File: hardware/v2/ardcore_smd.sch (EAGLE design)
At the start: 78 parts, among them IC10 TL072, IC11 74AHCT1G125DBV, IC2 7805DT, IC4 4921, IC5 74AHCT1G125DBV, IC6 ATMEGA328P-AU, IC7 74AHCT1G125DBV, IC8 74AHCT1G125DBV, Y1 RESONATORSMD

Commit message: New components
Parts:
- removed AUDIO_OUT: WQP-PJ301M-12_JACK, thonkiconn:WQP-PJ301M-12_JACK
- removed C21: 100p, rcl:C-USC0603
- removed C29: 47p, rcl:C-USC0603
- removed IC10: TL072, linear:TL072D
- removed R45, R46: 39k, rcl:R-US_R0603
- removed R50: 47k, rcl:R-US_R0603
- removed R55: 1.0k, rcl:R-US_R0603
- removed R56: 100k, rcl:R-US_R0603
- added AUDIO_OUT1, AUDIO_OUT2: WQP-PJ301M-12_JACK, thonkiconn:WQP-PJ301M-12_JACK
- added C11: 470n, rcl:C-USC0603
- added C14, C15, C19, C20: 220p, rcl:C-USC0603
- added C17, C23: 18p, rcl:C-USC0603
- added C8, C9: 100n, rcl:C-USC0603
- added IC1, IC3: OPA2171, linear:TL072D
- added IC12: LM4040B25, texas:LM4041B12DBZ
- added IC9: LM4040B10, texas:LM4041B12DBZ
- added L1: (no value), wuerth-elektronik:WE-CBF_0603
- added R12, R14, R17, R22, R24, R26: 39k, rcl:R-US_R0603
- added R18, R29: 249k, rcl:R-US_R0603
- added R19, R30: 309k, rcl:R-US_R0603
- added R20, R31: 1.0k, rcl:R-US_R0603
- added R25, R9: 3.3k, rcl:R-US_R0603
- added U2: DAC8552IDGKT, Texas Instruments_By_element14_Batch_1:DAC8552IDGKT
- C22: value 100p -> 470n
- C4: value 10u -> 22u; device rcl:CPOL-EUE2.5-5 -> rcl:CPOL-USC
- IC4: value 4921 -> LM1117-3.3; device adafruit_mcp:MCP4921SO08 -> og-vreg:REG1117
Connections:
- removed net N$67: C21.2, C4.+, IC10B.-IN, IC10B.OUT
- removed net N$68: C4.-, R50.2
- removed net N$69: C22.1, IC10B.+IN, R46.1
- removed net N$71: C21.1, R45.1, R46.2
- removed net N$72: AUDIO_OUT.2, R55.1, R56.1
- removed net N$73: C29.2, IC10A.OUT, R55.2
- removed net N$75: C29.1, IC10A.-IN, R50.1, R56.2
- new net +3V3: C4.+, C8.1, IC4.VOUT, L1.1
- new net +3V3_A: C9.1, L1.2, R9.1, U2.VDD
- new net A: R22.2, U2.VOUTA
- new net AREF_-10: C22.1, IC9.A, R19.2, R25.2, R30.2
- new net AREF_2.5: C11.1, IC12.C, R9.2, U2.VREF
- new net B: R12.2, U2.VOUTB
- new net BI_OUT: C17.2, IC1A.OUT, R18.1, R20.2
- new net BI_OUT1: C23.2, IC3A.OUT, R29.1, R31.2
- new net F_CV: C17.1, IC1A.-IN, R17.1, R18.2, R19.1
- new net F_CV1: C23.1, IC3A.-IN, R26.1, R29.2, R30.1
- new net N$1: C14.1, R12.1, R14.2
- new net N$24: C20.1, IC3B.+IN, R24.1
- new net N$26: C19.1, R22.1, R24.2
- new net N$32: AUDIO_OUT1.2, R31.1
- new net N$4: C19.2, IC3B.-IN, IC3B.OUT, R26.2
- new net N$42: C14.2, IC1B.-IN, IC1B.OUT, R17.2
- new net N$43: C15.1, IC1B.+IN, R14.1
- net +5V: no longer IC4.REFA, IC4.VDD
- net GND: now also AUDIO_OUT1.1, AUDIO_OUT2.1, C11.2, C15.2, C20.2, C4.-, C8.2, C9.2, IC12.A, IC1A.+IN, IC3A.+IN, IC4.GND, IC9.C, U2.GND; no longer AUDIO_OUT.1, IC10A.+IN, IC4.AVSS, IC4.LDAC
- net MOSI: no longer IC4.SDI
- net N$2: now also AUDIO_OUT2.2, R20.1; no longer IC4.DACA, R45.2
- net SCK: no longer IC4.SCK
- net SS: no longer IC4.#CS
- net VCC: now also IC1P.V+, IC3P.V+, IC4.VIN; no longer IC10P.V+
- net VEE: now also IC1P.V-, IC3P.V-, R25.1; no longer IC10P.V-
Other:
- note added: "+/-8V"
- note removed: "DAC alternatives: MCP4901 8bit MCP4911 10bit MCP4921 12bit"

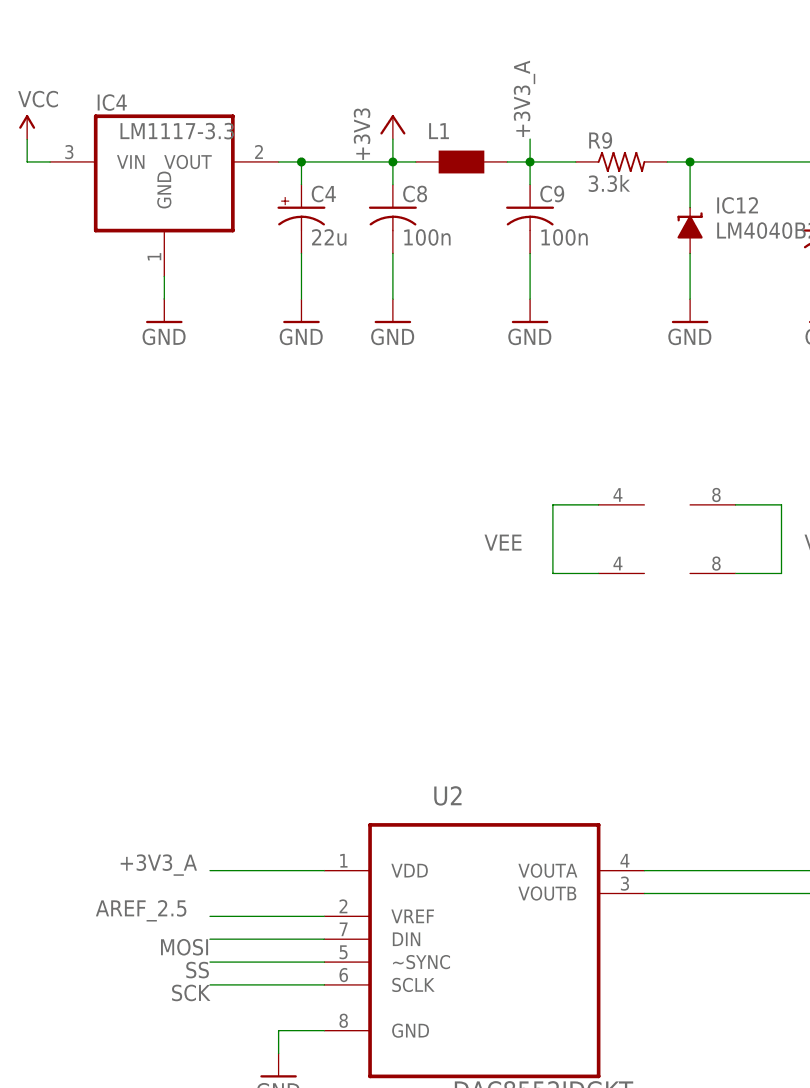
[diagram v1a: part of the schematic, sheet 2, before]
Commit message: removing 3v3 reg
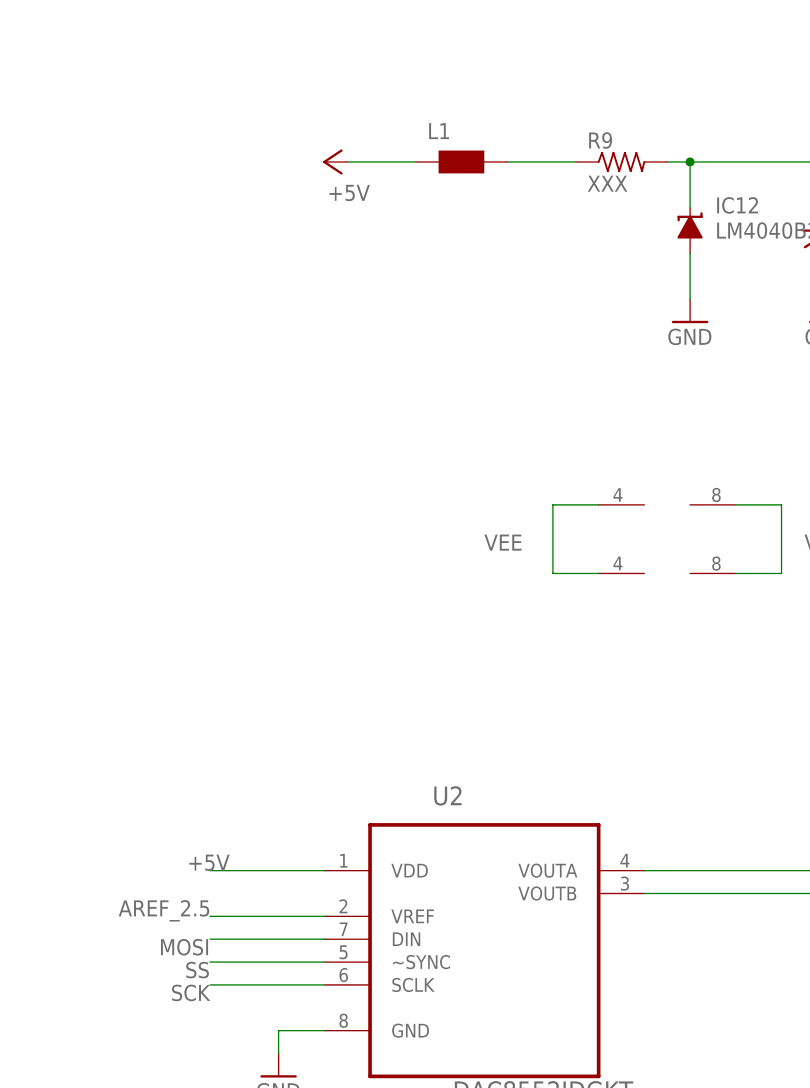
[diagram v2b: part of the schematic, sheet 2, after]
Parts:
- removed C4: 22u, rcl:CPOL-USC
- removed C8, C9: 100n, rcl:C-USC0603
- removed IC4: LM1117-3.3, og-vreg:REG1117
- R9: value 3.3k -> XXX
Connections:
- removed net +3V3: C4.+, C8.1, IC4.VOUT, L1.1
- removed net +3V3_A: C9.1, L1.2, R9.1, U2.VDD
- new net N$33: L1.2, R9.1
- net +5V: now also L1.1, U2.VDD
- net GND: no longer C4.-, C8.2, C9.2, IC4.GND
- net VCC: no longer IC4.VIN
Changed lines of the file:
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@@
 <?xml version="1.0" encoding="utf-8"?>
 <!DOCTYPE eagle SYSTEM "eagle.dtd">
-<eagle version="6.1">
+<eagle version="7.3.0">
 <drawing>
 <settings>
@@
 <part name="GND4" library="SparkFun" deviceset="GND" device=""/>
 <part name="GND14" library="SparkFun" deviceset="GND" device=""/>
-<part name="C4" library="rcl" deviceset="CPOL-US" device="C" value="22u"/>
-<part name="C8" library="rcl" deviceset="C-US" device="C0603" value="100n"/>
-<part name="GND16" library="SparkFun" deviceset="GND" device=""/>
-<part name="GND18" library="SparkFun" deviceset="GND" device=""/>
-<part name="GND36" library="SparkFun" deviceset="GND" device=""/>
-<part name="IC4" library="og-vreg" deviceset="REG1117" device="" value="LM1117-3.3"/>
-<part name="+3V1" library="supply1" deviceset="+3V3" device=""/>
-<part name="P+4" library="SparkFun" deviceset="VCC" device=""/>
 <part name="L1" library="wuerth-elektronik" deviceset="WE-CBF" device="_0603"/>
-<part name="C9" library="rcl" deviceset="C-US" device="C0603" value="100n"/>
-<part name="GND23" library="SparkFun" deviceset="GND" device=""/>
 <part name="IC9" library="texas" deviceset="LM4041" device="DBZ" technology="B12" value="LM4040B10"/>
 <part name="R25" library="rcl" deviceset="R-US_" device="R0603" value="3.3k"/>
@@
 <part name="SUPPLY3" library="supply2" deviceset="VEE" device=""/>
 <part name="IC12" library="texas" deviceset="LM4041" device="DBZ" technology="B12" value="LM4040B25"/>
-<part name="R9" library="rcl" deviceset="R-US_" device="R0603" value="3.3k"/>
+<part name="R9" library="rcl" deviceset="R-US_" device="R0603" value="XXX"/>
 <part name="GND24" library="SparkFun" deviceset="GND" device=""/>
 <part name="C11" library="rcl" deviceset="C-US" device="C0603" value="470n"/>
 <part name="GND25" library="SparkFun" deviceset="GND" device=""/>
 <part name="GND31" library="SparkFun" deviceset="GND" device=""/>
+<part name="P+10" library="supply1" deviceset="+5V" device=""/>
 </parts>
 <sheets>
@@
 <instance part="GND4" gate="1" x="233.68" y="71.12"/>
 <instance part="GND14" gate="1" x="236.22" y="10.16"/>
-<instance part="C4" gate="G$1" x="40.64" y="139.7"/>
-<instance part="C8" gate="G$1" x="50.8" y="139.7"/>
-<instance part="GND16" gate="1" x="25.4" y="127"/>
-<instance part="GND18" gate="1" x="40.64" y="127"/>
-<instance part="GND36" gate="1" x="50.8" y="127"/>
-<instance part="IC4" gate="G$1" x="25.4" y="144.78"/>
-<instance part="+3V1" gate="G$1" x="50.8" y="149.86"/>
-<instance part="P+4" gate="1" x="10.16" y="147.32"/>
 <instance part="L1" gate="G$1" x="58.42" y="142.24"/>
-<instance part="C9" gate="G$1" x="66.04" y="139.7"/>
-<instance part="GND23" gate="1" x="66.04" y="127"/>
 <instance part="IC9" gate="G$1" x="149.86" y="129.54" rot="R180"/>
 <instance part="R25" gate="G$1" x="149.86" y="144.78" rot="R270"/>
@@
 <instance part="IC3" gate="P" x="81.28" y="106.68" rot="R270"/>
 <instance part="IC1" gate="P" x="81.28" y="99.06" rot="R270"/>
+<instance part="P+10" gate="1" x="43.18" y="144.78" rot="R90"/>
 </instances>
 <busses>
@@
 <pinref part="AUDIO_OUT1" gate="G$1" pin="1"/>
 <wire x1="233.68" y1="78.74" x2="238.76" y2="78.74" width="0.1524" layer="91"/>
-</segment>
-<segment>
-<wire x1="25.4" y1="132.08" x2="25.4" y2="129.54" width="0.1524" layer="91"/>
-<pinref part="GND16" gate="1" pin="GND"/>
-<pinref part="IC4" gate="G$1" pin="GND"/>
-</segment>
-<segment>
-<wire x1="40.64" y1="134.62" x2="40.64" y2="129.54" width="0.1524" layer="91"/>
-<pinref part="C4" gate="G$1" pin="-"/>
-<pinref part="GND18" gate="1" pin="GND"/>
-</segment>
-<segment>
-<wire x1="50.8" y1="134.62" x2="50.8" y2="129.54" width="0.1524" layer="91"/>
-<pinref part="C8" gate="G$1" pin="2"/>
-<pinref part="GND36" gate="1" pin="GND"/>
-</segment>
-<segment>
-<wire x1="66.04" y1="134.62" x2="66.04" y2="129.54" width="0.1524" layer="91"/>
-<pinref part="C9" gate="G$1" pin="2"/>
-<pinref part="GND23" gate="1" pin="GND"/>
 </segment>
 <segment>
@@
 <net name="VCC" class="0">
 <segment>
-<wire x1="10.16" y1="144.78" x2="12.7" y2="144.78" width="0.1524" layer="91"/>
-<wire x1="10.16" y1="147.32" x2="10.16" y2="144.78" width="0.1524" layer="91"/>
-<pinref part="IC4" gate="G$1" pin="VIN"/>
-<pinref part="P+4" gate="1" pin="VCC"/>
-</segment>
-<segment>
 <pinref part="IC3" gate="P" pin="V+"/>
 <wire x1="88.9" y1="106.68" x2="93.98" y2="106.68" width="0.1524" layer="91"/>
@@
 <wire x1="88.9" y1="99.06" x2="93.98" y2="99.06" width="0.1524" layer="91"/>
 <wire x1="93.98" y1="99.06" x2="93.98" y2="106.68" width="0.1524" layer="91"/>
-</segment>
-</net>
-<net name="+3V3" class="0">
-<segment>
-<wire x1="38.1" y1="144.78" x2="40.64" y2="144.78" width="0.1524" layer="91"/>
-<wire x1="40.64" y1="144.78" x2="50.8" y2="144.78" width="0.1524" layer="91"/>
-<wire x1="40.64" y1="142.24" x2="40.64" y2="144.78" width="0.1524" layer="91"/>
-<wire x1="50.8" y1="147.32" x2="50.8" y2="144.78" width="0.1524" layer="91"/>
-<wire x1="53.34" y1="144.78" x2="50.8" y2="144.78" width="0.1524" layer="91"/>
-<wire x1="50.8" y1="142.24" x2="50.8" y2="144.78" width="0.1524" layer="91"/>
-<junction x="40.64" y="144.78"/>
-<junction x="50.8" y="144.78"/>
-<pinref part="C4" gate="G$1" pin="+"/>
-<pinref part="IC4" gate="G$1" pin="VOUT"/>
-<pinref part="+3V1" gate="G$1" pin="+3V3"/>
-<pinref part="L1" gate="G$1" pin="1"/>
-<pinref part="C8" gate="G$1" pin="1"/>
-</segment>
-</net>
-<net name="+3V3_A" class="0">
-<segment>
-<wire x1="63.5" y1="144.78" x2="66.04" y2="144.78" width="0.1524" layer="91"/>
-<wire x1="66.04" y1="144.78" x2="66.04" y2="142.24" width="0.1524" layer="91"/>
-<wire x1="66.04" y1="144.78" x2="66.04" y2="147.32" width="0.1524" layer="91"/>
-<wire x1="71.12" y1="144.78" x2="66.04" y2="144.78" width="0.1524" layer="91"/>
-<junction x="66.04" y="144.78"/>
-<label x="66.04" y="147.32" size="1.778" layer="95" rot="R90"/>
-<pinref part="L1" gate="G$1" pin="2"/>
-<pinref part="C9" gate="G$1" pin="1"/>
-<pinref part="R9" gate="G$1" pin="1"/>
-</segment>
-<segment>
-<pinref part="U2" gate="A" pin="VDD"/>
-<wire x1="43.18" y1="66.04" x2="30.48" y2="66.04" width="0.1524" layer="91"/>
-<label x="20.32" y="66.04" size="1.778" layer="95"/>
 </segment>
 </net>
@@
 <pinref part="U2" gate="A" pin="VREF"/>
 <wire x1="43.18" y1="60.96" x2="30.48" y2="60.96" width="0.1524" layer="91"/>
-<label x="17.78" y="60.96" size="1.778" layer="95"/>
+<label x="20.32" y="60.96" size="1.778" layer="95"/>
+</segment>
+</net>
+<net name="+5V" class="0">
+<segment>
+<pinref part="P+10" gate="1" pin="+5V"/>
+<pinref part="L1" gate="G$1" pin="1"/>
+<wire x1="45.72" y1="144.78" x2="53.34" y2="144.78" width="0.1524" layer="91"/>
+</segment>
+<segment>
+<pinref part="U2" gate="A" pin="VDD"/>
+<wire x1="43.18" y1="66.04" x2="30.48" y2="66.04" width="0.1524" layer="91"/>
+<label x="27.94" y="66.04" size="1.778" layer="95"/>
+</segment>
+</net>
+<net name="N$33" class="0">
+<segment>
+<pinref part="L1" gate="G$1" pin="2"/>
+<pinref part="R9" gate="G$1" pin="1"/>
+<wire x1="63.5" y1="144.78" x2="71.12" y2="144.78" width="0.1524" layer="91"/>
 </segment>
 </net>
@@
 </schematic>
 </drawing>
+<compatibility>
+<note version="6.3" minversion="6.2.2" severity="warning">
+Since Version 6.2.2 text objects can contain more than one line,
+which will not be processed correctly with this version.
+</note>
+</compatibility>
 </eagle>

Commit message: Adding version
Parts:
- IC12: value LM4040B25 -> LM4040
- IC9: value LM4040B10 -> LM4040
- U2: value DAC8552IDGKT -> DAC8552
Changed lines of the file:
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@@
 <?xml version="1.0" encoding="utf-8"?>
 <!DOCTYPE eagle SYSTEM "eagle.dtd">
-<eagle version="7.3.0">
+<eagle version="7.6.0">
 <drawing>
 <settings>
@@
 <part name="D7" library="hhn_diodes_smd" deviceset="LL4148" device=""/>
 <part name="D8" library="hhn_diodes_smd" deviceset="LL4148" device=""/>
-<part name="U2" library="Texas Instruments_By_element14_Batch_1" deviceset="DAC8552IDGKT" device=""/>
+<part name="U2" library="Texas Instruments_By_element14_Batch_1" deviceset="DAC8552IDGKT" device="" value="DAC8552"/>
 <part name="IC1" library="linear" deviceset="TL072" device="D" value="OPA2171"/>
 <part name="R12" library="rcl" deviceset="R-US_" device="R0603" value="39k"/>
@@
 <part name="GND14" library="SparkFun" deviceset="GND" device=""/>
 <part name="L1" library="wuerth-elektronik" deviceset="WE-CBF" device="_0603"/>
-<part name="IC9" library="texas" deviceset="LM4041" device="DBZ" technology="B12" value="LM4040B10"/>
+<part name="IC9" library="texas" deviceset="LM4041" device="DBZ" technology="B12" value="LM4040"/>
 <part name="R25" library="rcl" deviceset="R-US_" device="R0603" value="3.3k"/>
 <part name="C22" library="rcl" deviceset="C-US" device="C0603" value="470n"/>
 <part name="GND69" library="SparkFun" deviceset="GND" device=""/>
 <part name="SUPPLY3" library="supply2" deviceset="VEE" device=""/>
-<part name="IC12" library="texas" deviceset="LM4041" device="DBZ" technology="B12" value="LM4040B25"/>
+<part name="IC12" library="texas" deviceset="LM4041" device="DBZ" technology="B12" value="LM4040"/>
 <part name="R9" library="rcl" deviceset="R-US_" device="R0603" value="XXX"/>
 <part name="GND24" library="SparkFun" deviceset="GND" device=""/>

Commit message: changes on panel
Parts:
- added LED5, LED6, LED7: (no value), led:LED3MM
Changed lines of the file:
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@@
 <part name="GND31" library="SparkFun" deviceset="GND" device=""/>
 <part name="P+10" library="supply1" deviceset="+5V" device=""/>
+<part name="LED5" library="led" deviceset="LED" device="3MM"/>
+<part name="LED6" library="led" deviceset="LED" device="3MM"/>
+<part name="LED7" library="led" deviceset="LED" device="3MM"/>
 </parts>
 <sheets>
@@
 <instance part="D7" gate="G$1" x="269.24" y="205.74"/>
 <instance part="D8" gate="G$1" x="269.24" y="198.12" rot="R180"/>
+<instance part="LED5" gate="G$1" x="264.16" y="104.14" rot="R90"/>
+<instance part="LED6" gate="G$1" x="246.38" y="91.44" rot="R90"/>
+<instance part="LED7" gate="G$1" x="233.68" y="104.14" rot="R90"/>
 </instances>
 <busses>

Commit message: Adding v2 fixed gerbers
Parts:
- removed LED5, LED6, LED7: (no value), led:LED3MM
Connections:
- net MOSI: now also U2.DIN
- net SCK: now also U2.SCLK
- net SS: now also U2.~SYNC
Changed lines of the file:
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@@
 <part name="GND31" library="SparkFun" deviceset="GND" device=""/>
 <part name="P+10" library="supply1" deviceset="+5V" device=""/>
-<part name="LED5" library="led" deviceset="LED" device="3MM"/>
-<part name="LED6" library="led" deviceset="LED" device="3MM"/>
-<part name="LED7" library="led" deviceset="LED" device="3MM"/>
 </parts>
 <sheets>
@@
 <instance part="D7" gate="G$1" x="269.24" y="205.74"/>
 <instance part="D8" gate="G$1" x="269.24" y="198.12" rot="R180"/>
-<instance part="LED5" gate="G$1" x="264.16" y="104.14" rot="R90"/>
-<instance part="LED6" gate="G$1" x="246.38" y="91.44" rot="R90"/>
-<instance part="LED7" gate="G$1" x="233.68" y="104.14" rot="R90"/>
 </instances>
 <busses>
@@
 <wire x1="312.42" y1="172.72" x2="314.96" y2="172.72" width="0.1524" layer="91"/>
 <label x="317.5" y="172.72" size="1.778" layer="95"/>
-</segment>
-<segment>
-<wire x1="312.42" y1="187.96" x2="314.96" y2="187.96" width="0.1524" layer="91"/>
 </segment>
 <segment>
@@
 <wire x1="271.78" y1="198.12" x2="279.4" y2="198.12" width="0.1524" layer="91"/>
 <label x="281.94" y="198.12" size="1.778" layer="95" rot="R180"/>
+</segment>
+<segment>
+<wire x1="314.96" y1="213.36" x2="309.88" y2="213.36" width="0.1524" layer="91"/>
+<label x="304.8" y="210.82" size="1.778" layer="95"/>
+</segment>
+<segment>
+<wire x1="312.42" y1="187.96" x2="304.8" y2="187.96" width="0.1524" layer="91"/>
+<label x="302.26" y="185.42" size="1.778" layer="95"/>
+</segment>
+<segment>
+<wire x1="312.42" y1="162.56" x2="304.8" y2="162.56" width="0.1524" layer="91"/>
+<label x="302.26" y="160.02" size="1.778" layer="95"/>
+</segment>
+<segment>
+<wire x1="312.42" y1="137.16" x2="307.34" y2="137.16" width="0.1524" layer="91"/>
+<label x="302.26" y="134.62" size="1.778" layer="95"/>
 </segment>
 </net>
@@
 <wire x1="43.18" y1="58.42" x2="30.48" y2="58.42" width="0.1524" layer="91"/>
 <label x="30.48" y="58.42" size="1.778" layer="95" rot="R180"/>
+<pinref part="U2" gate="A" pin="DIN"/>
 </segment>
 </net>
@@
 <wire x1="43.18" y1="53.34" x2="30.48" y2="53.34" width="0.1524" layer="91"/>
 <label x="30.48" y="53.34" size="1.778" layer="95" rot="R180"/>
+<pinref part="U2" gate="A" pin="SCLK"/>
 </segment>
 </net>
@@
 <wire x1="43.18" y1="55.88" x2="30.48" y2="55.88" width="0.1524" layer="91"/>
 <label x="30.48" y="55.88" size="1.778" layer="95" rot="R180"/>
-</segment>
-</net>
+<pinref part="U2" gate="A" pin="~SYNC"/>
+</segment>
+</net>
